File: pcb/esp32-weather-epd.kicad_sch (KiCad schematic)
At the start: 67 parts, among them J1 S2B-PH-K-S(LF)(SN), Q1 S8050, Q2 S8050, Q3 BRCS150P02ZJ, Q4 SI1308EDL-T1-GE3, U1 CH340X, U2 TP4056X, U3 RT9080-33GJ5, U4 ESP32-WROOM-32E, U5 BME680

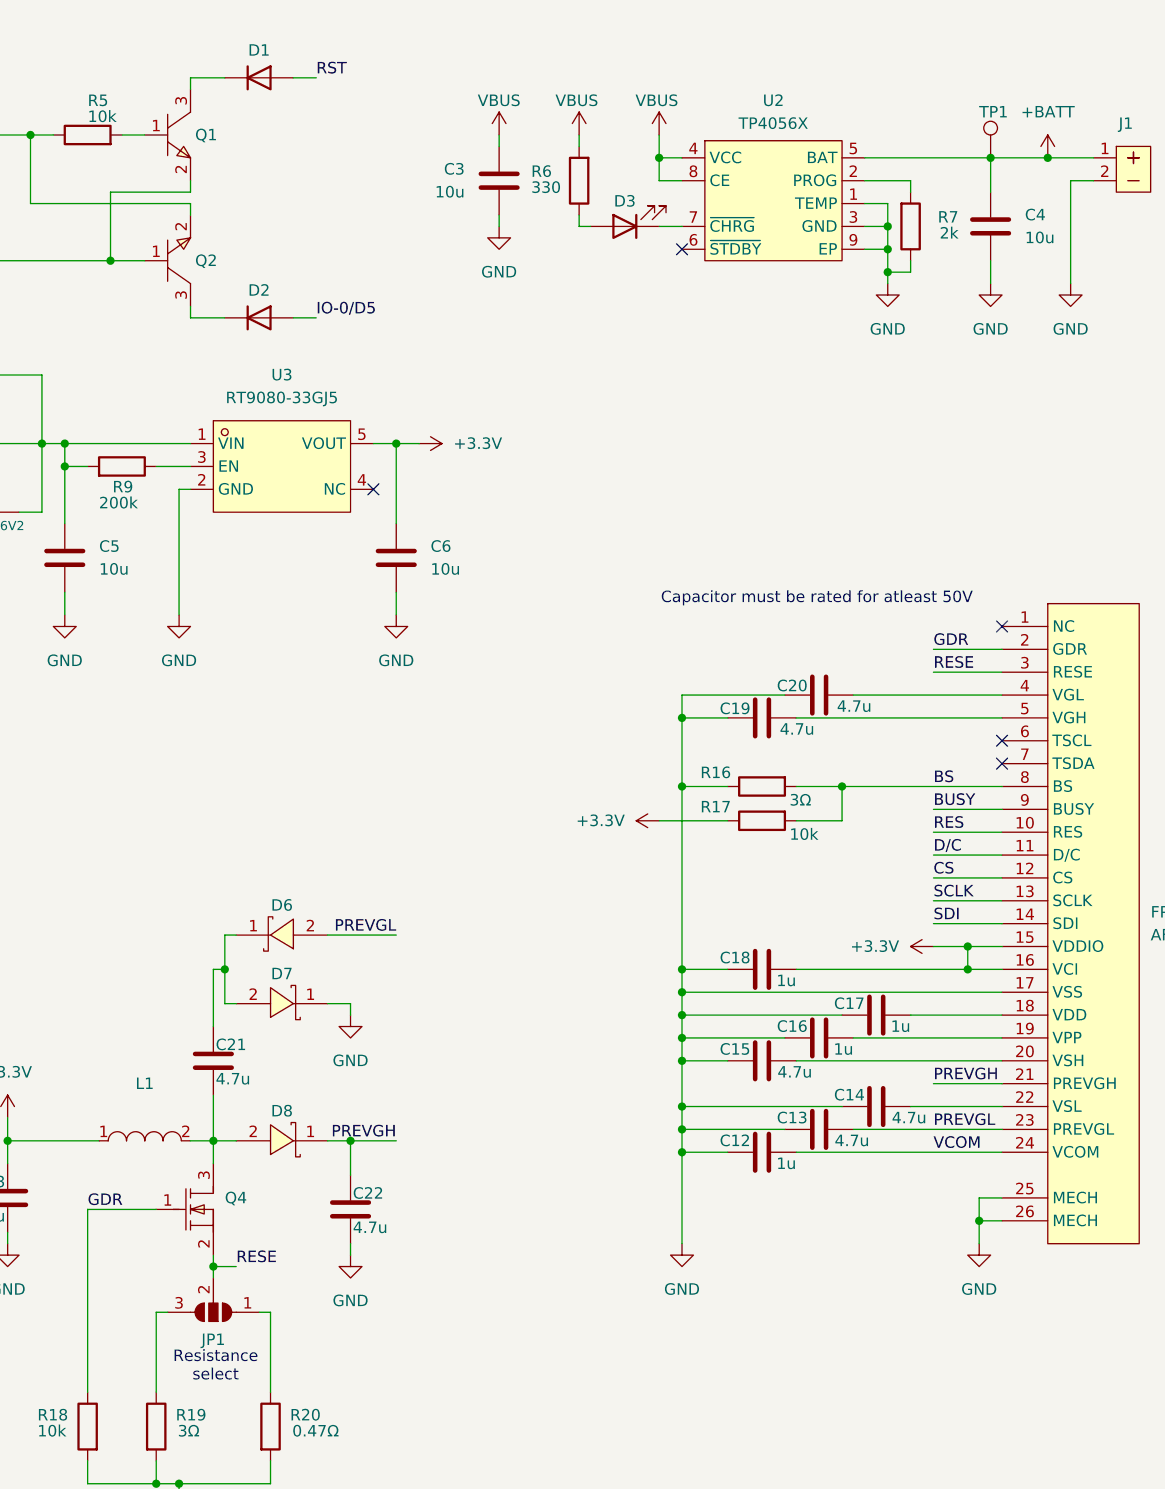
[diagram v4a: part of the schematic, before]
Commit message: add missing footprint and LCSC part number
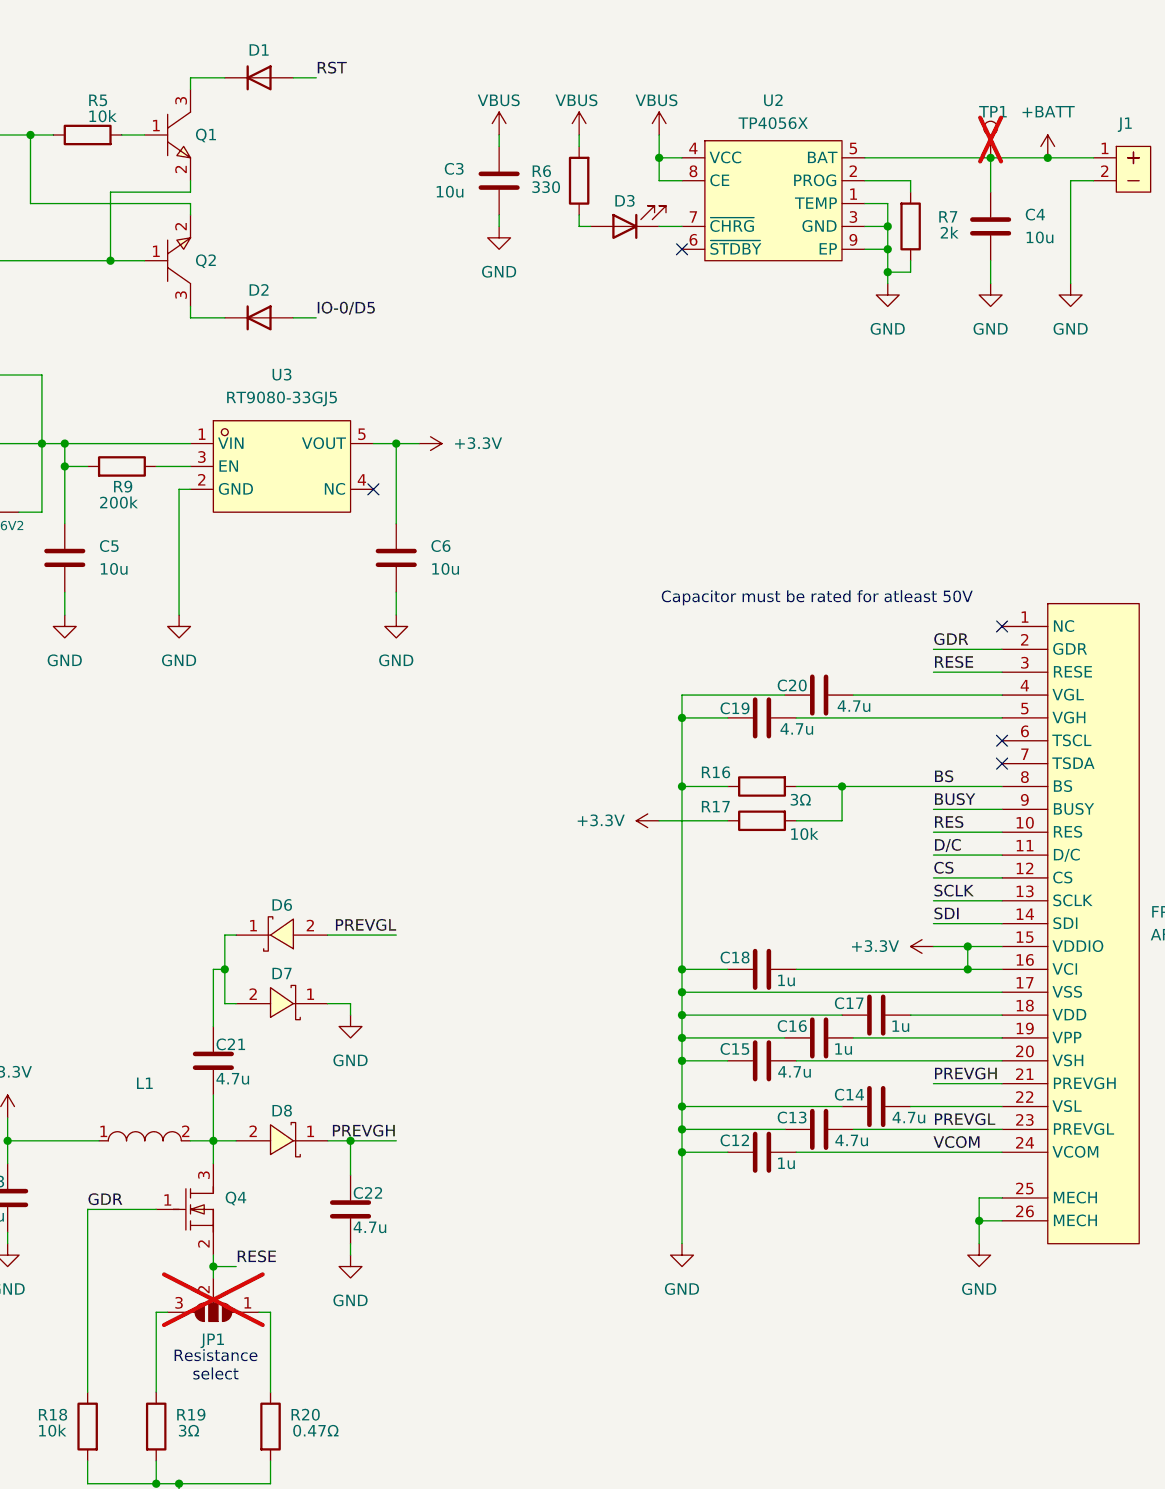
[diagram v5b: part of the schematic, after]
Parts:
- C1, C10, C11, C2, C7, C9: footprint (none) -> Capacitor_SMD:C_0603_1608Metric; LCSC Part (none) -> C14663
- C12, C16, C17, C18: footprint (none) -> Capacitor_SMD:C_0603_1608Metric; LCSC Part (none) -> C15849
- C13, C14, C15, C19, C20, C21, C22, C23: footprint (none) -> Capacitor_SMD:C_0805_2012Metric; LCSC Part (none) -> C98192
- C3, C4, C5, C6: footprint (none) -> Capacitor_SMD:C_0603_1608Metric; LCSC Part (none) -> C96446
- C8: footprint (none) -> Capacitor_SMD:C_0603_1608Metric; LCSC Part (none) -> C59461
- D1, D2: footprint (none) -> Diode_SMD:D_SOD-323; LCSC Part (none) -> C2128
- D3: LCSC Part (none) -> C397045
- D4: footprint (none) -> Diode_SMD:D_SOD-123F; LCSC Part (none) -> C169540
- D5: footprint (none) -> Diode_SMD:D_SOD-323; LCSC Part (none) -> C131806
- J1: footprint libs:CONN-TH_S2B-PH-K-S-LF-SN -> 0_local_lib:CONN-TH_S2B-PH-K-S-LF-SN
- JP1: now not fitted
- Q1, Q2: footprint libs:SOT-23-3_L2.9-W1.6-P1.90-LS2.8-BR -> 0_local_lib:SOT-23-3_L2.9-W1.6-P1.90-LS2.8-BR
- R1, R2: footprint (none) -> Resistor_SMD:R_0603_1608Metric; LCSC Part (none) -> C23186
- R10, R11, R12, R13: footprint (none) -> Resistor_SMD:R_0603_1608Metric; LCSC Part (none) -> C25803
- R14, R15: footprint (none) -> Resistor_SMD:R_0603_1608Metric; LCSC Part (none) -> C23162
- R16, R19: footprint (none) -> Resistor_SMD:R_0603_1608Metric; LCSC Part (none) -> C23157
- R17, R18, R5, R8: footprint (none) -> Resistor_SMD:R_0603_1608Metric; LCSC Part (none) -> C25804
- R20: footprint (none) -> Resistor_SMD:R_0603_1608Metric; LCSC Part (none) -> C23411
- R3: footprint (none) -> Resistor_SMD:R_0603_1608Metric; LCSC Part (none) -> C22962
- R4: footprint (none) -> Resistor_SMD:R_0603_1608Metric; LCSC Part (none) -> C4190
- R6: footprint (none) -> Resistor_SMD:R_0603_1608Metric; LCSC Part (none) -> C23138
- R7: footprint (none) -> Resistor_SMD:R_0603_1608Metric; LCSC Part (none) -> C22975
- R9: footprint (none) -> Resistor_SMD:R_0603_1608Metric; LCSC Part (none) -> C25811
- TP1: footprint (none) -> TestPoint:TestPoint_Pad_D1.0mm; now not fitted
- U1: footprint libs:MSOP-10_L3.0-W3.0-P0.50-LS5.0-BL -> 0_local_lib:MSOP-10_L3.0-W3.0-P0.50-LS5.0-BL
- U2: footprint libs:SOP-8_L4.9-W3.9-P1.27-LS6.0-TL-EP -> 0_local_lib:SOP-8_L4.9-W3.9-P1.27-LS6.0-TL-EP
- U3: footprint libs:SOT-23-5_L3.0-W1.5-P0.95-LS2.8-BL -> 0_local_lib:SOT-23-5_L3.0-W1.5-P0.95-LS2.8-BL
- U4: LCSC Part (none) -> C701341

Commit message: add missing rx and tx connection
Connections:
- net D0(RX): now also U4.34 (RXD0/IO3)
- net D1(TX): now also U4.35 (TXD0/IO1)
- no-connect marks 22 -> 20
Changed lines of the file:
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@@
-	)
-	(no_connect
-		(at 105.41 111.76)
 	)
 	(no_connect
@@
 		(at 48.26 29.21)
 	)
-	(no_connect
-		(at 105.41 106.68)
-	)
 	(wire
 		(pts
@@
 	(wire
 		(pts
+			(xy 105.41 111.76) (xy 113.03 111.76)
+		)
+		(stroke
+			(width 0)
+			(type default)
+		)
+	)
+	(wire
+		(pts
 			(xy 151.13 161.29) (xy 152.4 161.29)
 		)
@@
 	(wire
 		(pts
-			(xy 105.41 134.62) (xy 111.76 134.62)
+			(xy 105.41 134.62) (xy 113.03 134.62)
 		)
 		(stroke
@@
 	(wire
 		(pts
-			(xy 105.41 139.7) (xy 111.76 139.7)
+			(xy 105.41 139.7) (xy 113.03 139.7)
 		)
 		(stroke
@@
 	(wire
 		(pts
-			(xy 105.41 142.24) (xy 111.76 142.24)
+			(xy 105.41 142.24) (xy 113.03 142.24)
 		)
 		(stroke
@@
 	(wire
 		(pts
-			(xy 105.41 121.92) (xy 111.76 121.92)
+			(xy 105.41 121.92) (xy 113.03 121.92)
 		)
 		(stroke
@@
 	(wire
 		(pts
-			(xy 105.41 124.46) (xy 111.76 124.46)
+			(xy 105.41 124.46) (xy 113.03 124.46)
 		)
 		(stroke
@@
 	(wire
 		(pts
+			(xy 105.41 106.68) (xy 113.03 106.68)
+		)
+		(stroke
+			(width 0)
+			(type default)
+		)
+	)
+	(wire
+		(pts
 			(xy 48.26 128.27) (xy 48.26 129.54)
 		)
@@
 	(wire
 		(pts
-			(xy 105.41 132.08) (xy 111.76 132.08)
+			(xy 105.41 132.08) (xy 113.03 132.08)
 		)
 		(stroke
@@
 	(wire
 		(pts
-			(xy 105.41 144.78) (xy 111.76 144.78)
+			(xy 105.41 144.78) (xy 113.03 144.78)
 		)
 		(stroke
@@
 	)
 	(label "SDA"
-		(at 111.76 132.08 180)
+		(at 113.03 132.08 180)
 		(effects
 			(font
@@
 	)
 	(label "BUSY"
-		(at 111.76 124.46 180)
+		(at 113.03 124.46 180)
 		(effects
 			(font
@@
 	)
 	(label "SDI"
-		(at 111.76 144.78 180)
+		(at 113.03 144.78 180)
 		(effects
 			(font
@@
 	)
 	(label "SCLK"
-		(at 111.76 134.62 180)
+		(at 113.03 134.62 180)
+		(effects
+			(font
+				(size 1.27 1.27)
+			)
+			(justify right bottom)
+		)
+	)
+	(label "D1(TX)"
+		(at 113.03 106.68 180)
 		(effects
 			(font
@@
 	)
 	(label "SCL"
-		(at 111.76 129.54 180)
+		(at 113.03 129.54 180)
 		(effects
 			(font
@@
 		)
 	)
+	(label "D0(RX)"
+		(at 113.03 111.76 180)
+		(effects
+			(font
+				(size 1.27 1.27)
+			)
+			(justify right bottom)
+		)
+	)
 	(label "SDA"
 		(at 26.67 82.55 180)
@@
 	)
 	(label "RES"
-		(at 111.76 139.7 180)
+		(at 113.03 139.7 180)
 		(effects
 			(font
@@
 	)
 	(label "D{slash}C"
-		(at 111.76 142.24 180)
+		(at 113.03 142.24 180)
 		(effects
 			(font
@@
 	)
 	(label "CS"
-		(at 111.76 121.92 180)
-		(effects
-			(font
+		(at 113.03 121.92 180)
+		(effects
+			(font

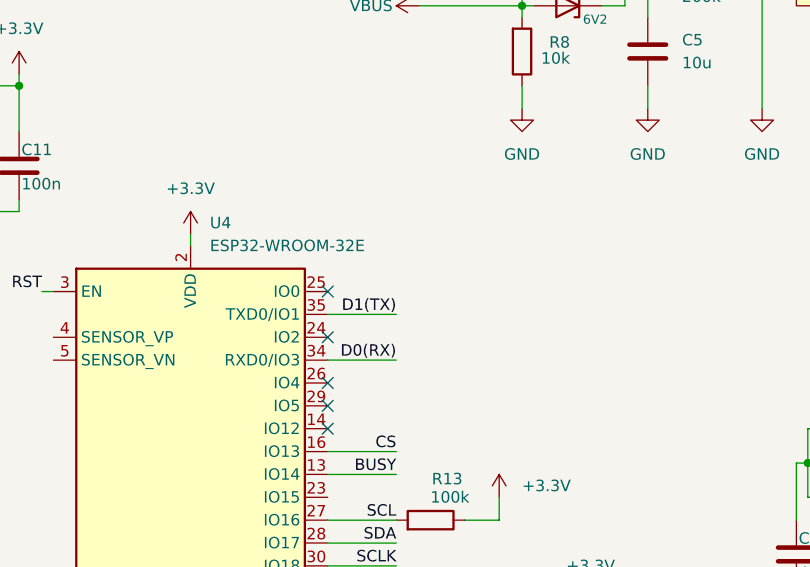
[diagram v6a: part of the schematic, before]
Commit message: add missing i0 connection
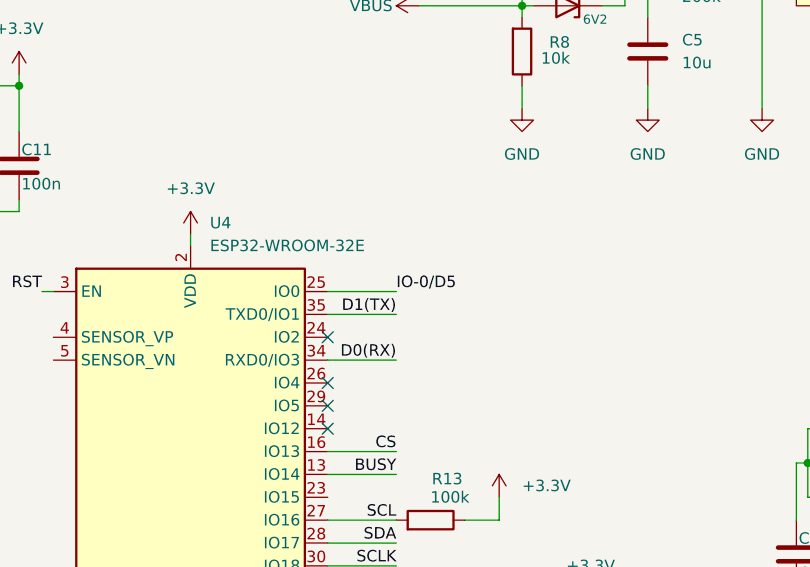
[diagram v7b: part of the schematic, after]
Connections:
- net IO-0/D5: now also U4.25 (IO0)
- no-connect marks 20 -> 19
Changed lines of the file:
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@@
-	)
-	(no_connect
-		(at 105.41 104.14)
 	)
 	(no_connect
@@
 		(pts
 			(xy 207.01 40.64) (xy 209.55 40.64)
+		)
+		(stroke
+			(width 0)
+			(type default)
+		)
+	)
+	(wire
+		(pts
+			(xy 105.41 104.14) (xy 113.03 104.14)
 		)
 		(stroke
@@
 		)
 	)
+	(label "IO-0{slash}D5"
+		(at 113.03 104.14 0)
+		(effects
+			(font
+				(size 1.27 1.27)
+			)
+			(justify left bottom)
+		)
+	)
